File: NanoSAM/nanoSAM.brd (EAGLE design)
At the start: 95.9 x 90.2 mm, 85 parts, among them J1 POWER_JACK, U1 LTC3260EMSEPBF

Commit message: Added Coin Cell Battery library, schematic, and board.
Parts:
- added U$20, U$21: CR2032, BatteryCR2032:CR2032
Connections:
- net -5V: now also U$20.P$1
- net 5V: now also U$21.P$2
- net AGND: now also U$20.P$2, U$21.P$1
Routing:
- net 5V: track 54.2 -> 70.9 mm
- net AGND: track 13.9 -> 25.0 mm, vias 17 -> 20
- net -5V: track 74.2 -> 81.2 mm
- removed copper zone on layer 2, net AGRD
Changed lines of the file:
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@@
 <attribute name="VALUE" x="66.94" y="73.957" size="1.778" layer="27" rot="R180"/>
 </element>
-<element name="H1" library="holes" library_urn="urn:adsk.eagle:library:237" package="3,6-PAD" package3d_urn="urn:adsk.eagle:package:14284/1" value="MOUNT-PAD-ROUND3.6" x="5.08" y="8.9" smashed="yes"/>
-<element name="H2" library="holes" library_urn="urn:adsk.eagle:library:237" package="3,6-PAD" package3d_urn="urn:adsk.eagle:package:14284/1" value="MOUNT-PAD-ROUND3.6" x="90.8" y="85.1" smashed="yes"/>
-<element name="H3" library="holes" library_urn="urn:adsk.eagle:library:237" package="3,6-PAD" package3d_urn="urn:adsk.eagle:package:14284/1" value="MOUNT-PAD-ROUND3.6" x="90.8" y="5.08" smashed="yes"/>
-<element name="H4" library="holes" library_urn="urn:adsk.eagle:library:237" package="3,6-PAD" package3d_urn="urn:adsk.eagle:package:14284/1" value="MOUNT-PAD-ROUND3.6" x="5.08" y="82.6" smashed="yes"/>
+<element name="H1" library="holes" library_urn="urn:adsk.eagle:library:237" package="3,6-PAD" package3d_urn="urn:adsk.eagle:package:14284/1" value="MOUNT-PAD-ROUND3.6" x="5.08" y="8.9" smashed="yes">
+<attribute name="POPULARITY" value="0" x="5.08" y="8.9" size="1.778" layer="27" display="off"/>
+</element>
+<element name="H2" library="holes" library_urn="urn:adsk.eagle:library:237" package="3,6-PAD" package3d_urn="urn:adsk.eagle:package:14284/1" value="MOUNT-PAD-ROUND3.6" x="90.8" y="85.1" smashed="yes">
+<attribute name="POPULARITY" value="0" x="90.8" y="85.1" size="1.778" layer="27" display="off"/>
+</element>
+<element name="H3" library="holes" library_urn="urn:adsk.eagle:library:237" package="3,6-PAD" package3d_urn="urn:adsk.eagle:package:14284/1" value="MOUNT-PAD-ROUND3.6" x="90.8" y="5.08" smashed="yes">
+<attribute name="POPULARITY" value="0" x="90.8" y="5.08" size="1.778" layer="27" display="off"/>
+</element>
+<element name="H4" library="holes" library_urn="urn:adsk.eagle:library:237" package="3,6-PAD" package3d_urn="urn:adsk.eagle:package:14284/1" value="MOUNT-PAD-ROUND3.6" x="5.08" y="82.6" smashed="yes">
+<attribute name="POPULARITY" value="0" x="5.08" y="82.6" size="1.778" layer="27" display="off"/>
+</element>
 <element name="TP7" library="testpoint" package="1X01" value="" x="29" y="74" smashed="yes" rot="R90">
 <attribute name="NAME" x="31.27" y="77.603" size="1.778" layer="25" font="vector" ratio="20" rot="R180"/>
@@
 <attribute name="PROD_ID" value=" " x="77.7" y="82" size="1.778" layer="27" rot="R270" display="off"/>
 <attribute name="VALUE" x="80.557" y="82" size="1.778" layer="27" font="vector" ratio="20" rot="R270" align="top-center"/>
+</element>
+<element name="U$20" library="BatteryCR2032" package="CR2032" value="CR2032" x="12" y="50" smashed="yes" rot="MR90">
+<attribute name="NAME" x="4.38" y="48.73" size="1.27" layer="26" rot="MR90"/>
+</element>
+<element name="U$21" library="BatteryCR2032" package="CR2032" value="CR2032" x="12" y="27" smashed="yes" rot="MR90">
+<attribute name="NAME" x="4.38" y="25.73" size="1.27" layer="26" rot="MR90"/>
 </element>
 </elements>
@@
 <wire x1="18" y1="69" x2="18" y2="69.675" width="0.508" layer="1"/>
 <wire x1="18" y1="69.675" x2="17.815" y2="69.86" width="0.508" layer="1"/>
+<contactref element="U$21" pad="P$2"/>
+<wire x1="12" y1="38.1" x2="8.36" y2="34.46" width="0.508" layer="16"/>
+<wire x1="8.36" y1="34.46" x2="8.36" y2="22.9064" width="0.508" layer="16"/>
+<wire x1="8.36" y1="22.61" x2="8.36" y2="22.9064" width="0" layer="19" extent="16-16"/>
 </signal>
 <signal name="AGND">
@@
 <wire x1="16.2256" y1="17.40943125" x2="17.65943125" y2="17.40943125" width="0.254" layer="1"/>
 <wire x1="17.65943125" y1="17.40943125" x2="18.41" y2="18.16" width="0.254" layer="1"/>
+<contactref element="U$20" pad="P$2"/>
+<contactref element="U$21" pad="P$1"/>
+<via x="12" y="27" extent="1-16" drill="0.35"/>
+<via x="12" y="32" extent="1-16" drill="0.35"/>
+<polygon width="0.254" layer="2">
+<vertex x="32" y="17"/>
+<vertex x="32" y="9"/>
+<vertex x="37" y="9"/>
+<vertex x="37" y="17"/>
+</polygon>
+<via x="12" y="55" extent="1-16" drill="0.35"/>
+<wire x1="12" y1="61.1" x2="12" y2="55" width="0.508" layer="16"/>
+<wire x1="12" y1="32" x2="12" y2="27" width="0.508" layer="16"/>
 </signal>
 <signal name="DGND">
@@
 <wire x1="24.39" y1="27.61" x2="19.55" y2="27.61" width="0.508" layer="1"/>
 <wire x1="26.59" y1="25.41" x2="24.39" y2="27.61" width="0.508" layer="1"/>
-<wire x1="19.55" y1="27.61" x2="13" y2="34.16" width="0.508" layer="16"/>
-<wire x1="13" y1="79" x2="13" y2="34.16" width="0.508" layer="16"/>
+<wire x1="15.23" y1="79.73" x2="20.3" y2="74.66" width="0.508" layer="16"/>
+<wire x1="19.55" y1="27.61" x2="20.3" y2="28.36" width="0.508" layer="16"/>
+<wire x1="20.3" y1="74.66" x2="20.3" y2="48" width="0.508" layer="16"/>
 <contactref element="U$1" pad="2"/>
 <contactref element="U$3" pad="4"/>
+<wire x1="20.3" y1="48" x2="20.3" y2="28.36" width="0.508" layer="16"/>
 <wire x1="15.275" y1="75.06" x2="15.23" y2="75.105" width="0.2" layer="1"/>
-<wire x1="15.23" y1="79.73" x2="13.73" y2="79.73" width="0.508" layer="16"/>
-<wire x1="13.73" y1="79.73" x2="13" y2="79" width="0.508" layer="16"/>
 <wire x1="15.23" y1="75.105" x2="15.23" y2="79.73" width="0.508" layer="1"/>
+<contactref element="U$20" pad="P$1"/>
+<wire x1="12" y1="50" x2="18.3" y2="50" width="0.508" layer="16"/>
+<wire x1="18.3" y1="50" x2="20.3" y2="48" width="0.508" layer="16"/>
 </signal>
 <signal name="N$22">
@@
 <wire x1="59.6" y1="83.4" x2="59.6" y2="83.5" width="0.254" layer="1"/>
 </signal>
-<signal name="AGRD">
-<polygon width="0.254" layer="2">
-<vertex x="32" y="17"/>
-<vertex x="32" y="9"/>
-<vertex x="37" y="9"/>
-<vertex x="37" y="17"/>
-</polygon>
-</signal>
 </signals>

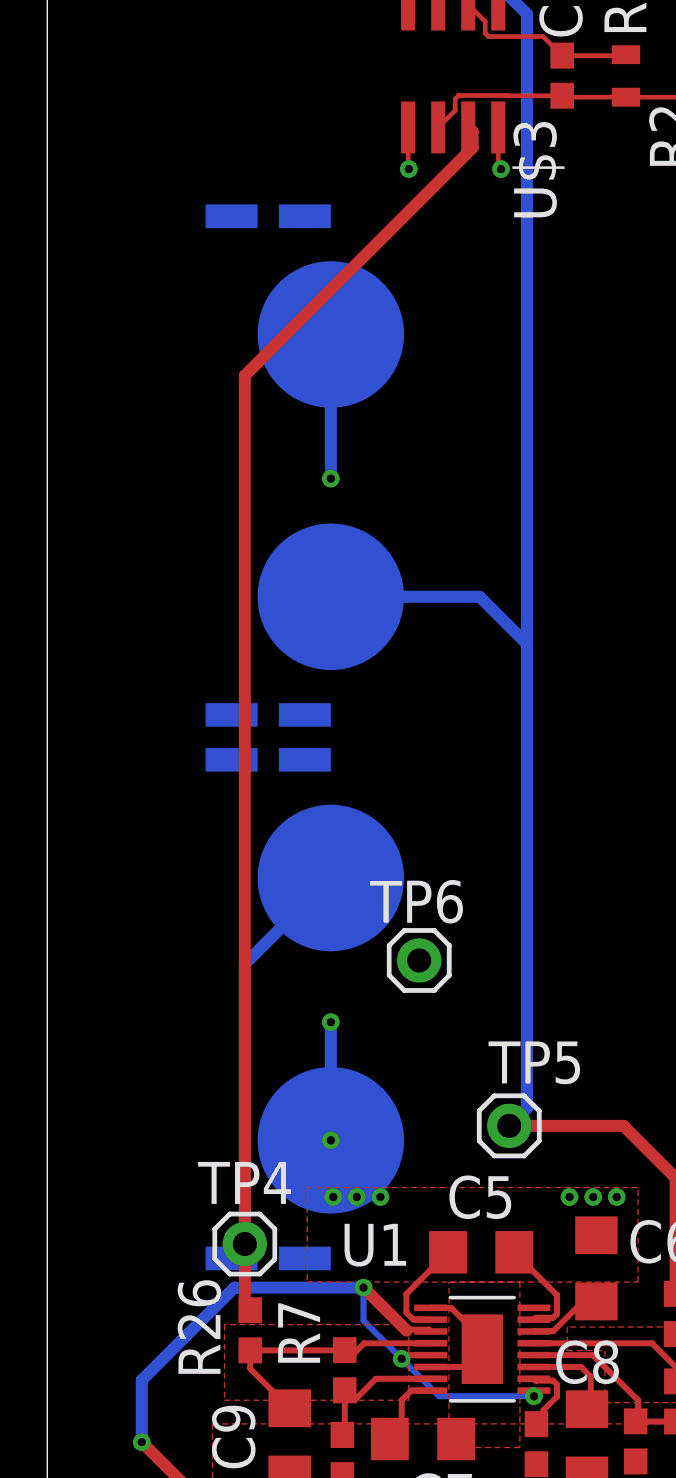
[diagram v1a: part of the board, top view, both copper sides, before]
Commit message: added some documentation to schematic, added datasheets folder
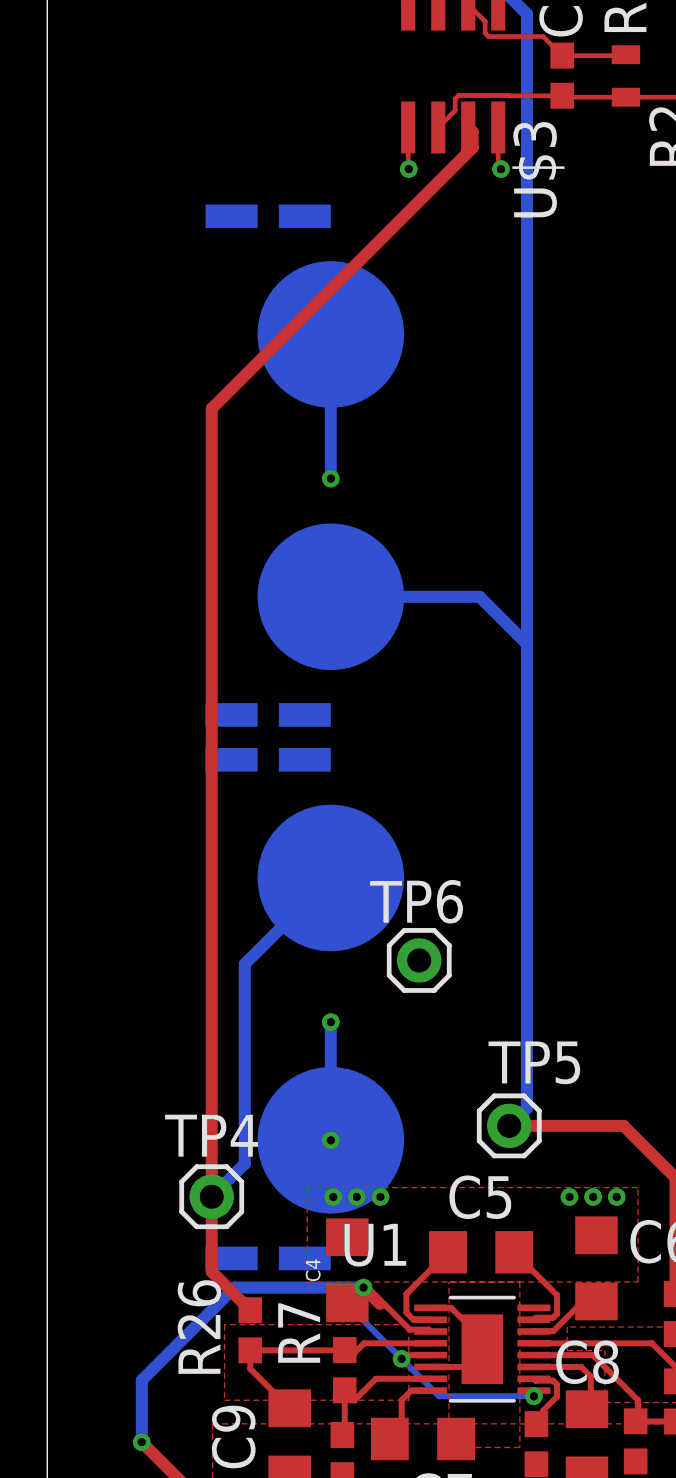
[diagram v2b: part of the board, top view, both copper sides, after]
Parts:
- added C4: 4.7uF, SparkFun-Capacitors:1206
- R25: value DNP -> 1M
- moved TP4 2.44 mm to (6.96, 24.6)
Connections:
- net AGND: now also C4.2
- net N$15: now also C4.1
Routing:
- net N$15: track 57.9 -> 57.3 mm
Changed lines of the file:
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@@
 <?xml version="1.0" encoding="utf-8"?>
 <!DOCTYPE eagle SYSTEM "eagle.dtd">
-<eagle version="9.5.1">
+<eagle version="9.3.0">
 <drawing>
 <settings>
@@
 <attribute name="VALUE" x="82.48" y="19.162" size="1.778" layer="27" font="vector" ratio="20" rot="R180" align="top-center"/>
 </element>
-<element name="R25" library="SparkFun-Resistors" library_urn="urn:adsk.eagle:library:532" package="0805" package3d_urn="urn:adsk.eagle:package:39651/1" value="DNP" x="24.49" y="72.04" smashed="yes" rot="R270">
+<element name="R25" library="SparkFun-Resistors" library_urn="urn:adsk.eagle:library:532" package="0805" package3d_urn="urn:adsk.eagle:package:39651/1" value="1M" x="24.49" y="72.04" smashed="yes" rot="R270">
 <attribute name="NAME" x="23.579" y="75.84" size="1.778" layer="25" font="vector" ratio="20" rot="R270" align="bottom-center"/>
 <attribute name="PROD_ID" value=" " x="-35.2" y="56.8" size="1.778" layer="27" rot="R270" display="off"/>
@@
 <attribute name="VALUE" x="60.9" y="11.186" size="0.6096" layer="27" font="vector" ratio="20" align="top-left"/>
 </element>
-<element name="TP4" library="testpoint" package="1X01" value="" x="8.36" y="22.61" smashed="yes">
-<attribute name="NAME" x="6.39" y="24.307" size="1.778" layer="25" font="vector" ratio="20"/>
-<attribute name="VALUE" x="7.09" y="21.086" size="0.6096" layer="27" font="vector" ratio="20" align="top-left"/>
+<element name="TP4" library="testpoint" package="1X01" value="" x="6.96" y="24.61" smashed="yes">
+<attribute name="NAME" x="4.99" y="26.307" size="1.778" layer="25" font="vector" ratio="20"/>
+<attribute name="VALUE" x="5.69" y="23.086" size="0.6096" layer="27" font="vector" ratio="20" align="top-left"/>
 </element>
 <element name="TP5" library="testpoint" package="1X01" value="" x="19.55" y="27.61" smashed="yes">
@@
 <element name="U$21" library="BatteryCR2032" package="CR2032" value="CR2032" x="12" y="27" smashed="yes" rot="MR90">
 <attribute name="NAME" x="4.38" y="25.73" size="1.27" layer="26" rot="MR90"/>
+</element>
+<element name="C4" library="SparkFun-Capacitors" library_urn="urn:adsk.eagle:library:510" package="1206" package3d_urn="urn:adsk.eagle:package:37426/1" value="4.7uF" x="12.7" y="21.5" smashed="yes" rot="R90">
+<attribute name="NAME" x="11.557" y="21.5" size="0.6096" layer="25" font="vector" ratio="20" rot="R90" align="bottom-center"/>
+<attribute name="PROD_ID" value="CAP-10300" x="12.7" y="21.5" size="1.778" layer="27" rot="R90" display="off"/>
+<attribute name="VALUE" x="13.843" y="21.5" size="0.6096" layer="27" font="vector" ratio="20" rot="R90" align="top-center"/>
 </element>
 </elements>
@@
 <contactref element="TP4" pad="1"/>
 <contactref element="R26" pad="2"/>
-<wire x1="8.59" y1="19.81" x2="8.36" y2="20.04" width="0.508" layer="1"/>
-<wire x1="8.36" y1="20.04" x2="8.36" y2="22.61" width="0.508" layer="1"/>
-<wire x1="8.36" y1="22.61" x2="8.36" y2="59.36" width="0.508" layer="1"/>
-<wire x1="8.36" y1="59.36" x2="18" y2="69" width="0.508" layer="1"/>
+<wire x1="8.59" y1="19.81" x2="6.96" y2="21.44" width="0.508" layer="1"/>
+<wire x1="6.96" y1="21.44" x2="6.96" y2="24.61" width="0.508" layer="1"/>
+<wire x1="6.96" y1="24.61" x2="6.96" y2="57.96" width="0.508" layer="1"/>
+<wire x1="6.96" y1="57.96" x2="18" y2="69" width="0.508" layer="1"/>
 <wire x1="18" y1="69" x2="18" y2="69.675" width="0.508" layer="1"/>
 <wire x1="18" y1="69.675" x2="17.815" y2="69.86" width="0.508" layer="1"/>
 <contactref element="U$21" pad="P$2"/>
 <wire x1="12" y1="38.1" x2="8.36" y2="34.46" width="0.508" layer="16"/>
-<wire x1="8.36" y1="34.46" x2="8.36" y2="22.9064" width="0.508" layer="16"/>
-<wire x1="8.36" y1="22.61" x2="8.36" y2="22.9064" width="0" layer="19" extent="16-16"/>
+<wire x1="8.36" y1="34.46" x2="8.36" y2="26.01" width="0.508" layer="16"/>
+<wire x1="8.36" y1="26.01" x2="6.96" y2="24.61" width="0.508" layer="16"/>
 </signal>
 <signal name="AGND">
@@
 <polygon width="0.254" layer="2">
 <vertex x="32" y="17"/>
-<vertex x="32" y="9"/>
-<vertex x="37" y="9"/>
-<vertex x="37" y="17"/>
+<vertex x="32" y="15"/>
+<vertex x="36.8" y="15"/>
+<vertex x="36.8" y="17"/>
 </polygon>
 <via x="12" y="55" extent="1-16" drill="0.35"/>
 <wire x1="12" y1="61.1" x2="12" y2="55" width="0.508" layer="16"/>
 <wire x1="12" y1="32" x2="12" y2="27" width="0.508" layer="16"/>
+<contactref element="C4" pad="2"/>
 </signal>
 <signal name="DGND">
@@
 <wire x1="13.38285625" y1="20.7664" x2="7.9216625" y2="20.7664" width="0.508" layer="16"/>
 <wire x1="13.38285625" y1="20.7664" x2="14.074628125" y2="20.074628125" width="0.508" layer="1"/>
-<wire x1="14.074628125" y1="20.074628125" x2="15.2056625" y2="18.94359375" width="0.508" layer="1"/>
 <wire x1="16.14431875" y1="18.99185" x2="16.2256" y2="18.91056875" width="0.254" layer="1"/>
 <wire x1="14.074628125" y1="20.074628125" x2="14.254234375" y2="20.074628125" width="0.254" layer="1"/>
@@
 <wire x1="14.9965" y1="17.7525875" x2="13.38285625" y2="19.36623125" width="0.254" layer="16"/>
 <wire x1="13.38285625" y1="19.36623125" x2="13.38285625" y2="20.7664" width="0.254" layer="16"/>
+<contactref element="C4" pad="1"/>
+<wire x1="12.7" y1="20.1" x2="12.71645625" y2="20.1" width="0.508" layer="1"/>
+<wire x1="12.71645625" y1="20.1" x2="13.38285625" y2="20.7664" width="0.508" layer="1"/>
 </signal>
 <signal name="N$16">
@@
 <mfgpreviewcolor name="substratecolor" color="0xFF786E46"/>
 </mfgpreviewcolors>
+<errors>
+</errors>
 </board>
 </drawing>

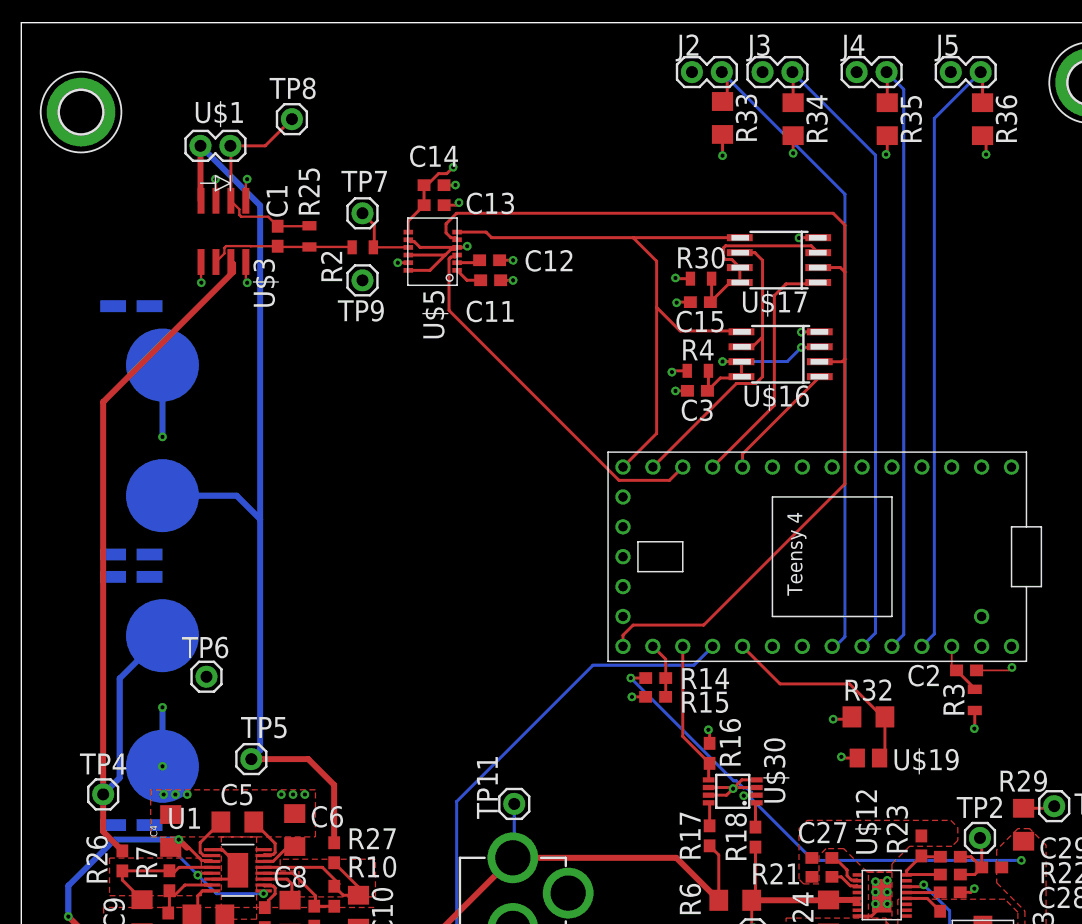
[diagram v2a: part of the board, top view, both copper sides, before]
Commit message: added unity gain op-amp buffer for instrument housekeeping
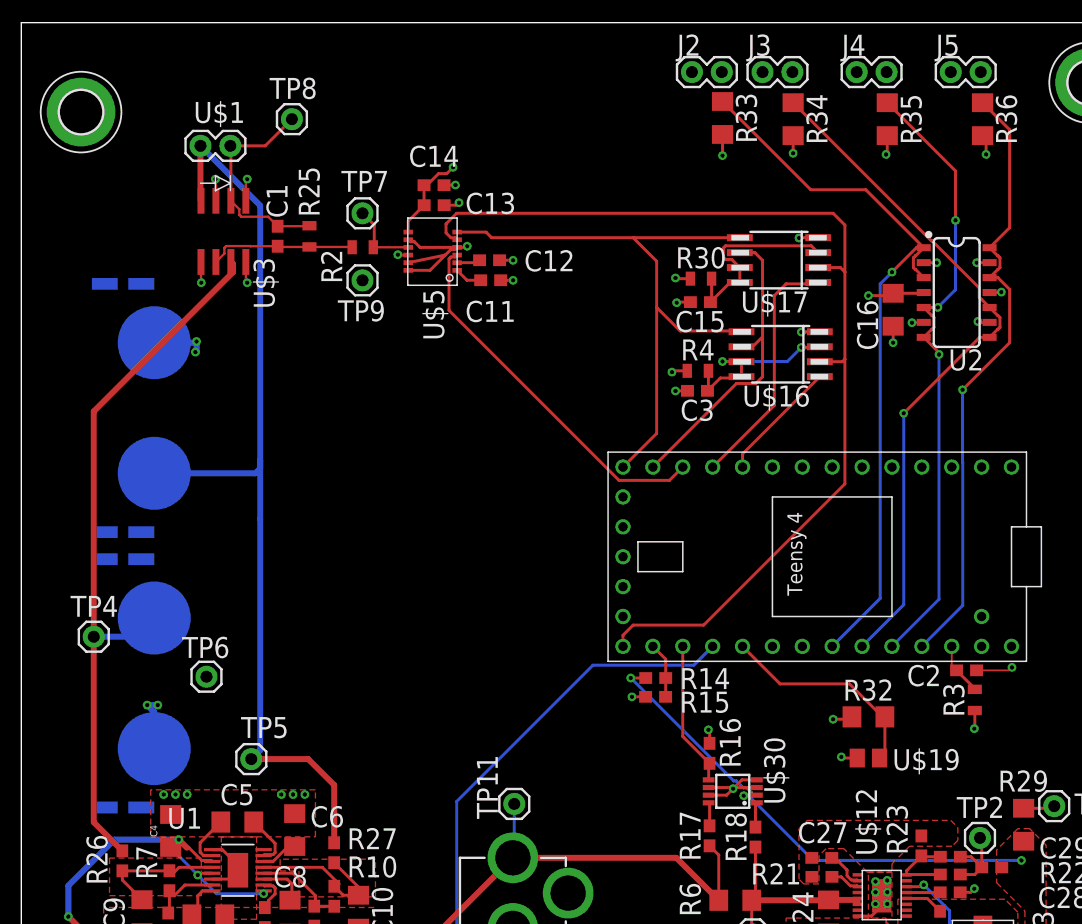
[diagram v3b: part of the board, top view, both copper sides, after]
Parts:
- added C16: .1uF, SparkFun-Capacitors:1206
- added U2: LMV324, SparkFun-IC-Amplifiers:SO14
- moved TP4 13.4 mm to (6.16, 38.0)
- moved U$20 2.02 mm to (11.3, 51.9)
- moved U$21 1.66 mm to (11.3, 28.5)
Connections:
- net +3V3: now also C16.1, U2.4
- net AGND: now also U$5.P10; no longer U$5.P11
- net DGND: now also C16.2, U$5.P11, U2.11, U2.13, U2.2, U2.6, U2.9; no longer U$5.P10
- net HK_INST_THRM0: now also U2.1, U2.3
- net HK_INST_THRM1: now also U2.10, U2.8
- net HK_INST_THRM2: now also U2.5, U2.7
- net HK_INST_THRM3: now also U2.12, U2.14
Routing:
- net 5V: track 71.0 -> 61.8 mm
- net DGND: track 52.8 -> 59.5 mm, vias 30 -> 36
- net HK_INST_THRM0: track 57.7 -> 63.0 mm, vias 0 -> 1
- net +3V3: track 29.5 -> 34.3 mm, vias 11 -> 12
- net HK_INST_THRM1: track 54.8 -> 58.9 mm, vias 0 -> 1
- net AGND: track 25.0 -> 23.3 mm, vias 20 -> 21
- net HK_INST_THRM2: track 52.5 -> 53.4 mm, vias 0 -> 3
- net -5V: track 81.2 -> 81.9 mm
- net HK_INST_THRM3: track 53.5 -> 52.8 mm, vias 0 -> 1
